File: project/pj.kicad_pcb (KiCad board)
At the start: 2 copper layers, 65 x 56.5 mm, 13 parts, among them J1 RPi_GPIO, J10 Pico PWR enable, J2 2B+, J3 zero, J4 3A+, J5 3B+, J6 4, J7 Conn_01x02, J8 Conn_01x02, J9 External PWR, SW1 SW_Push, SW2 SW_Push

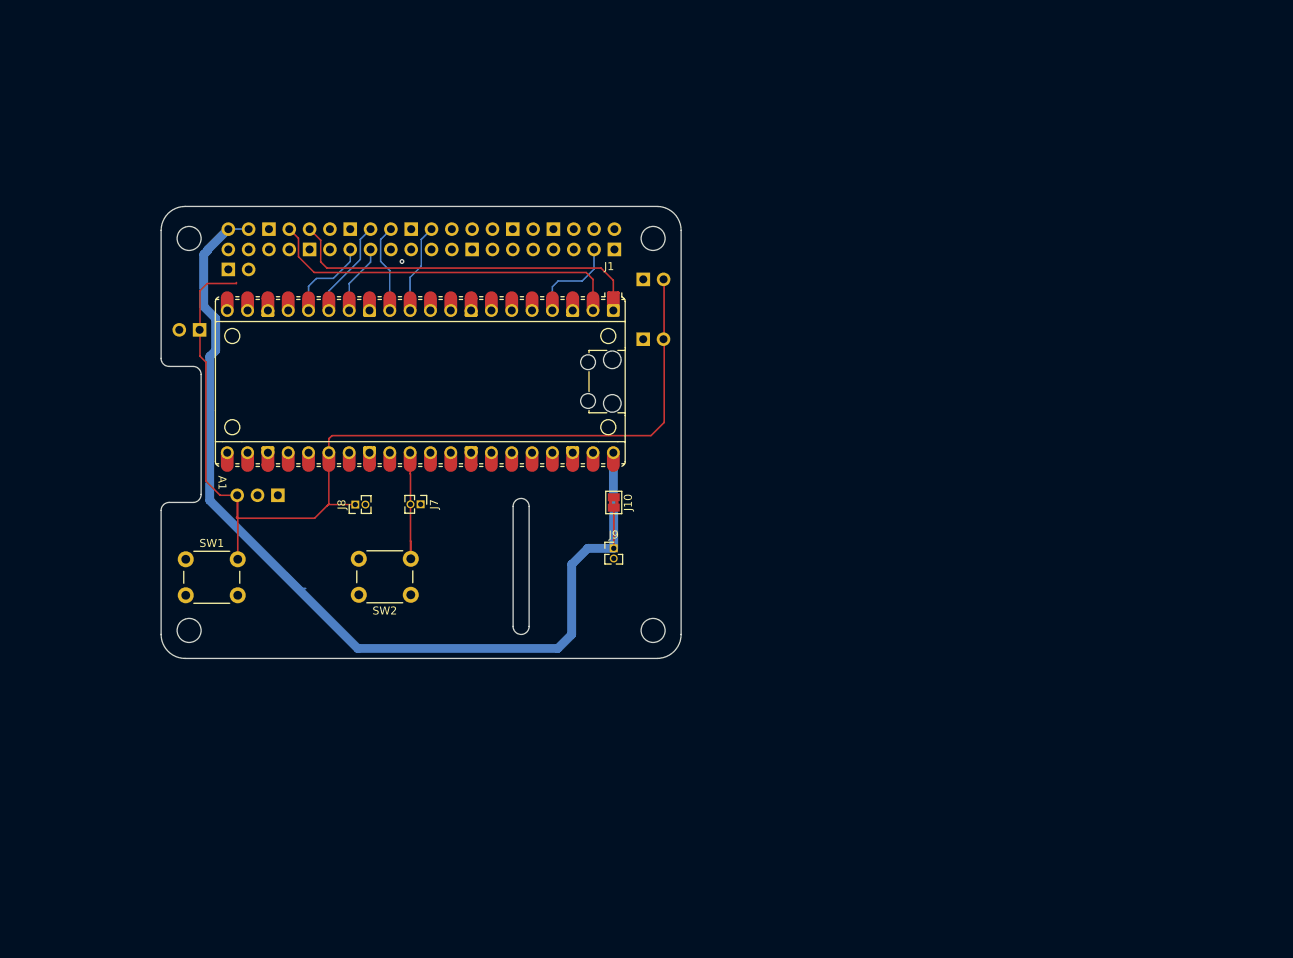
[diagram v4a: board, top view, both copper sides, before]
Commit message: add JTAG pin labels
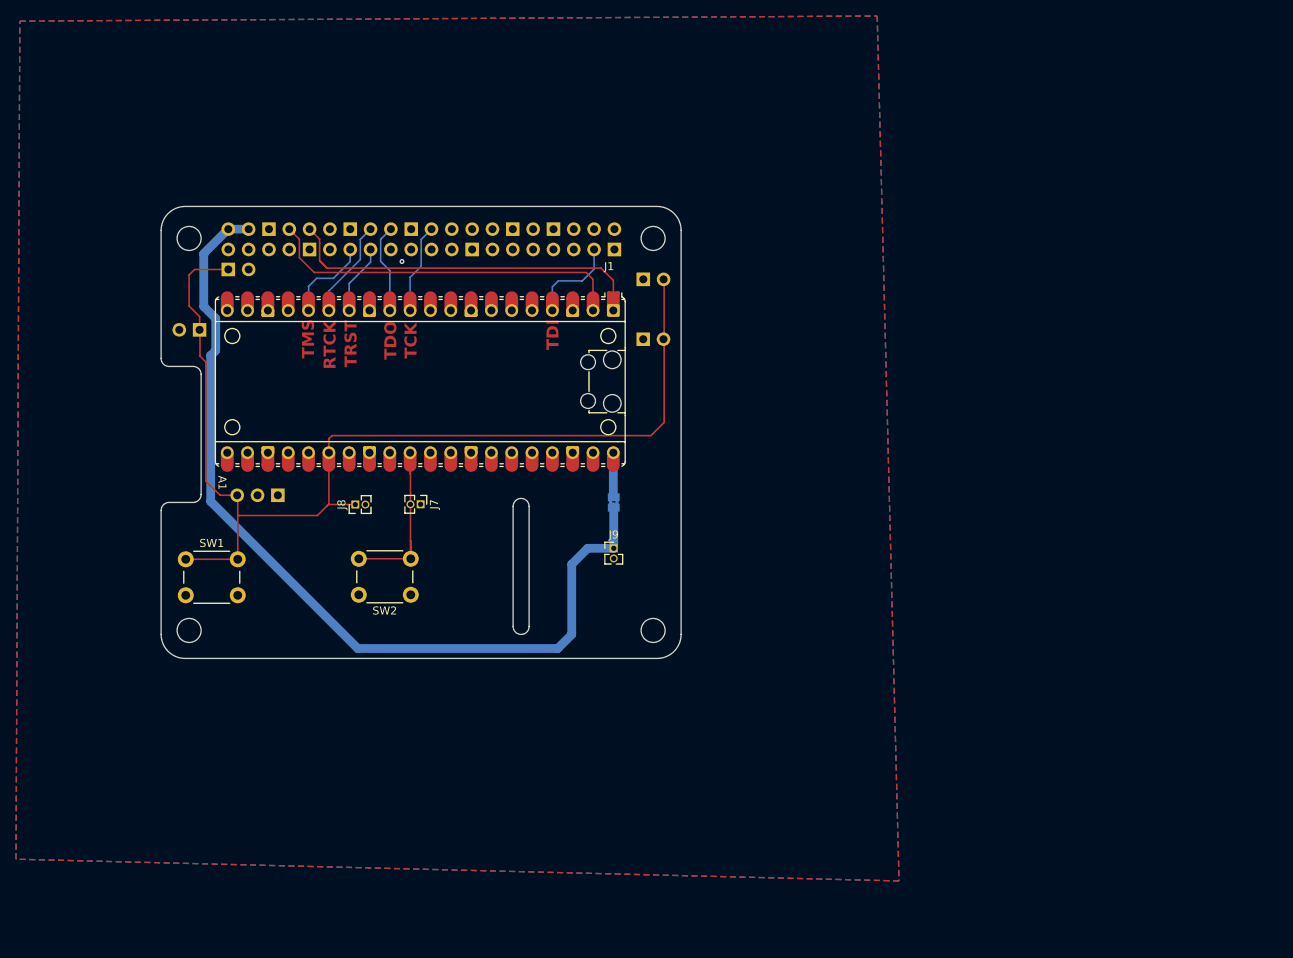
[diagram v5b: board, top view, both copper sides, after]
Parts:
- J10: moved to B.Cu
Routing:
- net Net-(J10-Pin_2): track 119.8 -> 112.3 mm
- net Net-(A1-RUN): track 15.5 -> 22.0 mm
- net Net-(A1-GPIO20): track 129.4 -> 135.3 mm
- net Net-(A1-GPIO0): track 46.0 -> 47.5 mm
- net Net-(A1-VBUS): track 6.24 -> 5.53 mm
- added copper zone on B.Cu, net GND
- added copper zone on F.Cu, net GND
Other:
- board text added: "RTCK"
- board text added: "TCK"
- board text added: "TDI"
- board text added: "TDO"
- board text added: "TMS"
- board text added: "TRST"

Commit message: beacon
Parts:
- added D1: Beacon, LED_SMD:LED_0603_1608Metric, F.Cu at (48.0, 93.8)
- added R1: 4.7k, Resistor_SMD:R_0603_1608Metric, F.Cu at (53.5, 93.8)
- moved SW2 1.59 mm to (67.6, 90.6)
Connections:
- A1 pad 2: Net-(A1-GPIO1) -> unconnected-(A1-GPIO1-Pad2)
- A1 pad 29: unconnected-(A1-GPIO22-Pad29) -> Net-(A1-GPIO22)
- J1 pad 8: Net-(A1-GPIO1) -> unconnected-(J1-BCM14_TXD-Pad8)
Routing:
- net Net-(A1-GPIO1): track 45.8 -> 0.00 mm
- net (no net): track 0.00 -> 45.8 mm
- net Net-(A1-GPIO22): track 0.00 -> 27.8 mm
- net Net-(D1-A): track 0.00 -> 3.91 mm
- net Net-(A1-RUN): track 22.0 -> 23.5 mm

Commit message: oshw logo
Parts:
- added REF**: OSHW-Logo_5.7x6mm_SilkScreen, Symbol:OSHW-Logo_5.7x6mm_SilkScreen, F.Cu at (92.6, 90.1)
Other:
- board text added: "github.com/CarlFK/pj v1.0"

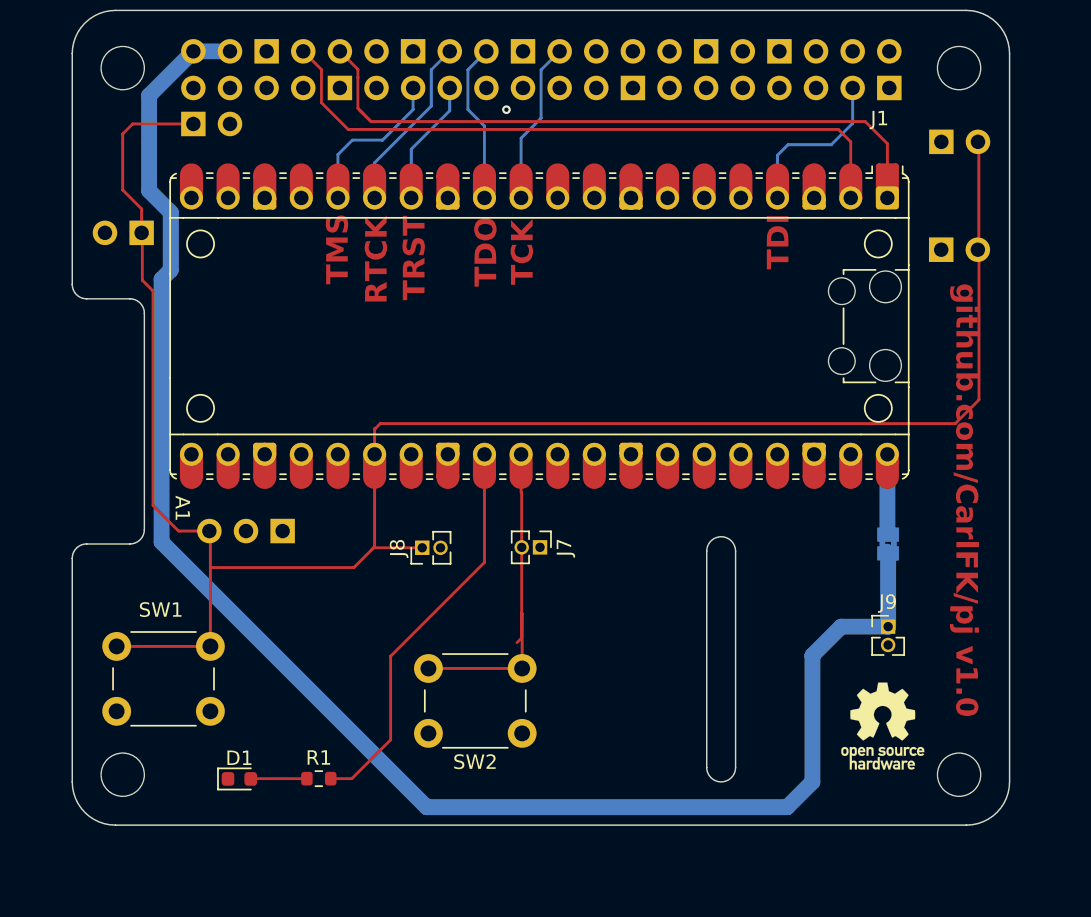
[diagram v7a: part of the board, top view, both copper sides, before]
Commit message: add gpio bus, lables and KiCad logo
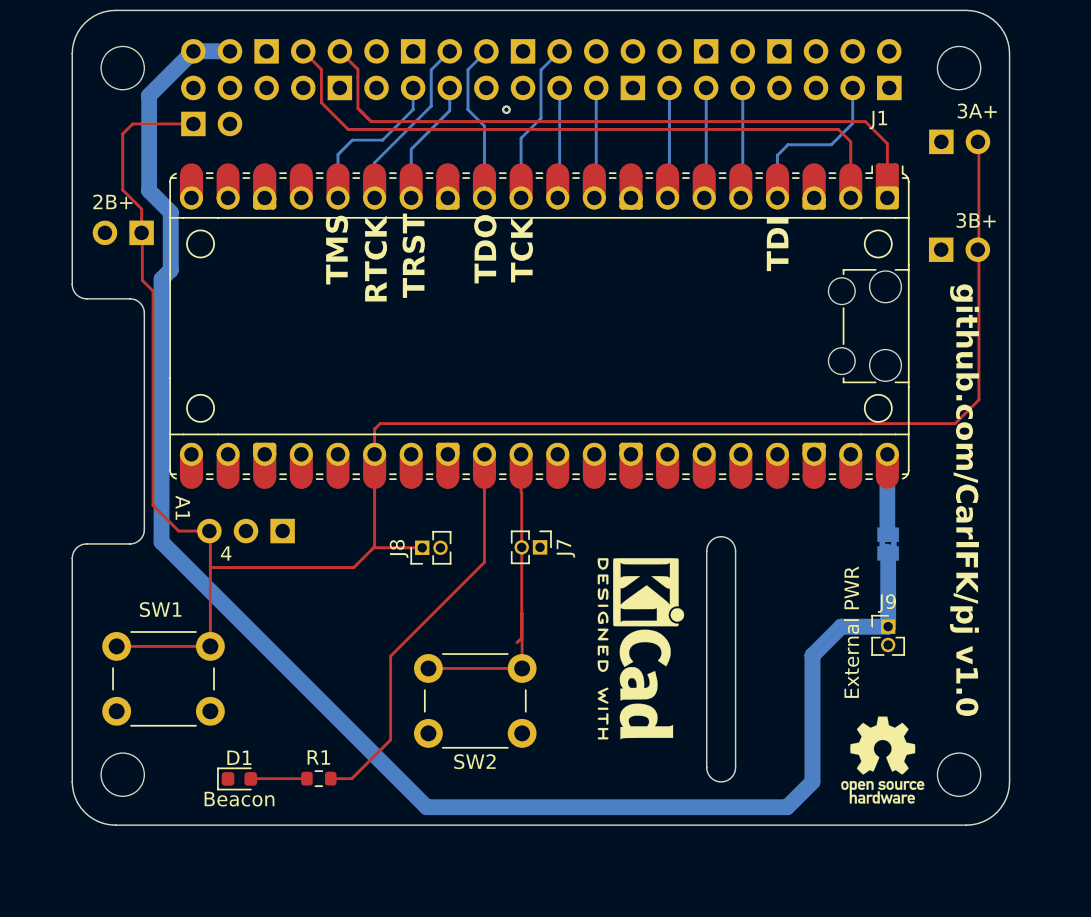
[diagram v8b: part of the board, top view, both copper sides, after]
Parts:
- added REF**: KiCad-Logo2_5mm_SilkScreen, Symbol:KiCad-Logo2_5mm_SilkScreen, F.Cu at (75.9, 84.8)
- J10: value Pico PWR enable -> PWR enable
- moved REF** 2.36 mm to (92.6, 92.5)
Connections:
- A1 pad 10: unconnected-(A1-GPIO7-Pad10) -> /b5
- A1 pad 5: unconnected-(A1-GPIO3-Pad5) -> /b1
- A1 pad 6: unconnected-(A1-GPIO4-Pad6) -> /b2
- A1 pad 7: unconnected-(A1-GPIO5-Pad7) -> /b3
- A1 pad 9: unconnected-(A1-GPIO6-Pad9) -> /b4
- J1 pad 21: unconnected-(J1-BCM9_MISO-Pad21) -> /b5
- J1 pad 23: unconnected-(J1-BCM11_SCLK-Pad23) -> /b4
- J1 pad 27: unconnected-(J1-BCM0_ID_SD-Pad27) -> /b3
- J1 pad 29: unconnected-(J1-BCM5-Pad29) -> /b2
- J1 pad 31: unconnected-(J1-BCM6-Pad31) -> /b1
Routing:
- net /b4: track 0.00 -> 7.68 mm
- net /b3: track 0.00 -> 7.68 mm
- net /b1: track 0.00 -> 7.68 mm
- net /b5: track 0.00 -> 7.68 mm
- net /b2: track 0.00 -> 7.68 mm
